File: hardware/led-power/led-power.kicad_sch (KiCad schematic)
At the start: 86 parts, among them J1 String1, J10 Conn_01x05_Male, J11 Qwiic, J12 Qwiic, J16 I2C Header, J17 IRQ, J2 String2, J3 String3, J4 String4, J5 String5, J6 String6, J7 String7, J8 String8, J9 PowerInput, Q1 Q_NMOS_GDS, Q2 Q_NMOS_GDS, Q3 Q_NMOS_GDS, Q4 Q_NMOS_GDS, Q5 Q_NMOS_GDS, Q6 Q_NMOS_GDS, Q7 Q_NMOS_GDS, Q8 Q_NMOS_GDS, U1 MCP6V51, U10 L78L05ACZ-AP, U11 MCP1501, U12 LM317_TO-220, U2 MCP6V51, U3 MCP6V51, U4 MCP6V51, U5 MCP6V51, U6 MCP6V51, U7 MCP6V51, U8 MCP6V51, U9 STM32G030Fx

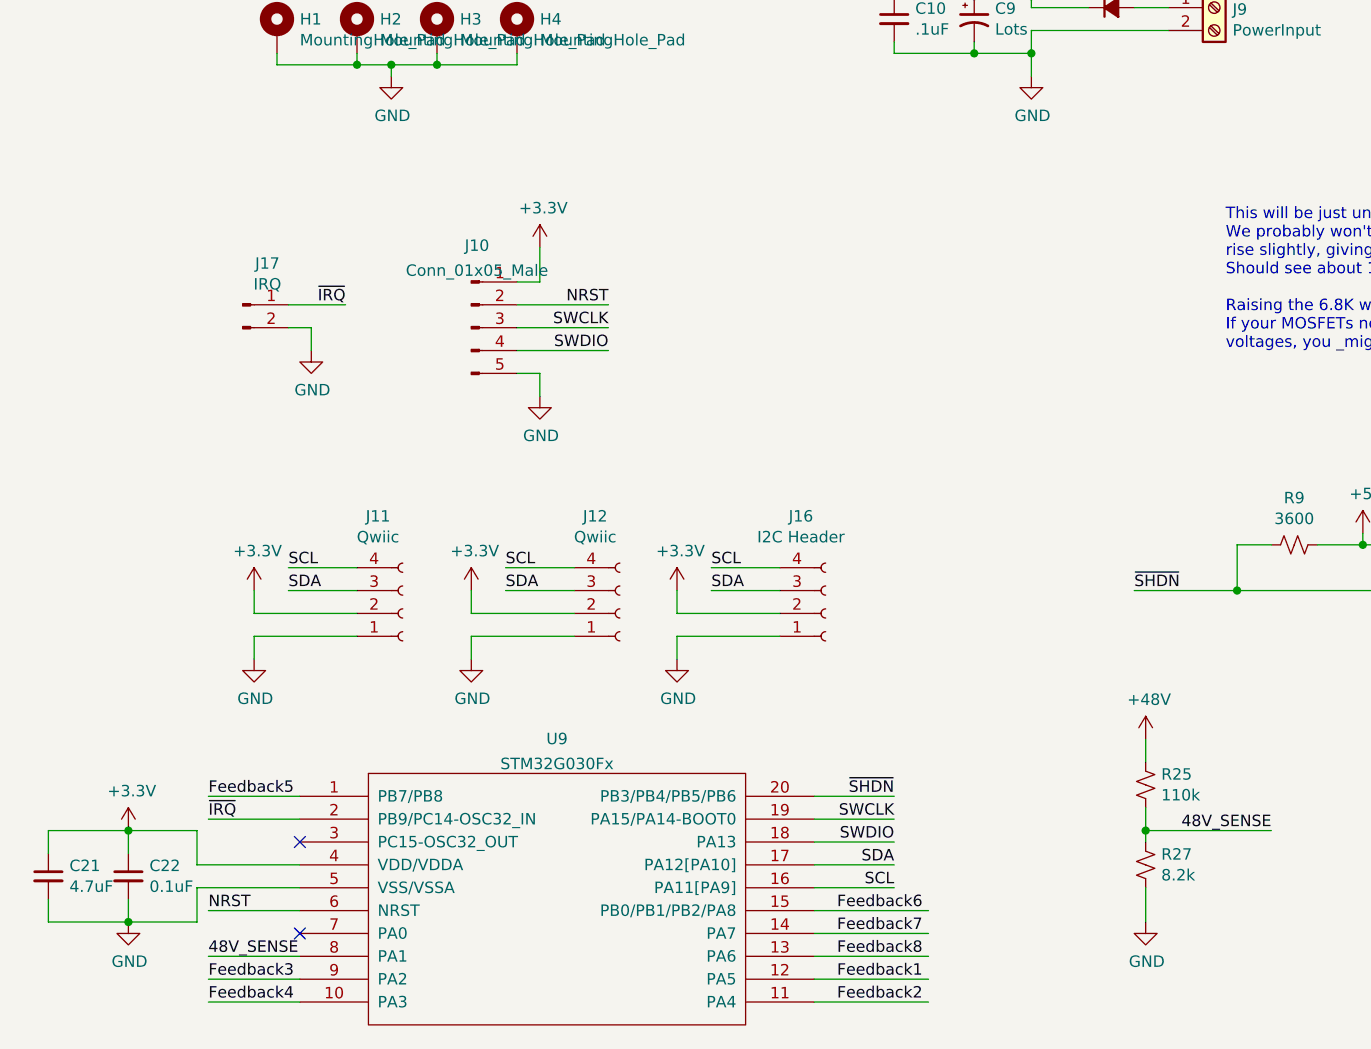
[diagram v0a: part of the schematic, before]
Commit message: Use a BJT to pull down the /IRQ line.
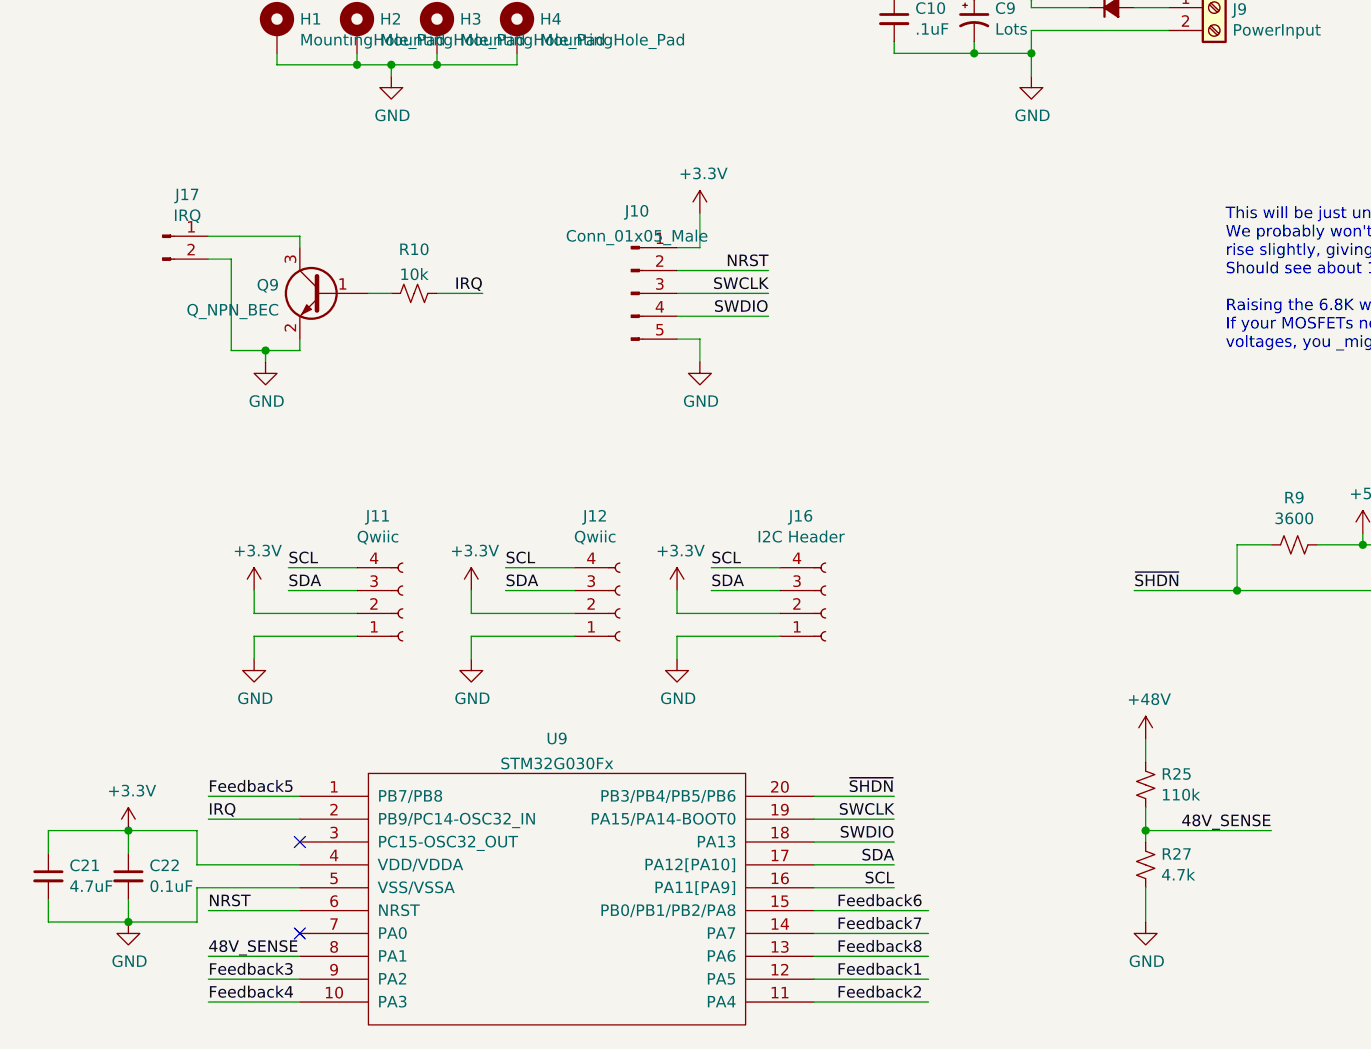
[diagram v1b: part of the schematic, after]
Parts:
- added Q9: Q_NPN_BEC, Package_TO_SOT_SMD:SOT-23, symbol Device:Q_NPN_BEC
- added R10: 10k, Resistor_SMD:R_0805_2012Metric_Pad1.20x1.40mm_HandSolder, symbol Device:R_Small_US
- R27: value 8.2k -> 4.7k
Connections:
- net GND: now also Q9.2 (E)
- net ~{IRQ}: no longer names the net of J17.1 (Pin_1)
- net ~{IRQ}: now also Q9.3 (C); no longer U9.2 (PB9/PC14-OSC32_IN)
- new net: Q9.1 (B), R10.1
- new net IRQ: R10.2, U9.2 (PB9/PC14-OSC32_IN)
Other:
- moved on the sheet: J10, J17

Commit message: Convert all other mounting holes to non-pad variety.
Reroute a few traces to be shorter.
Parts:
- H1, H2, H3, H4: footprint Mounting_Holes:MountingHole_3.2mm_M3_Pad_Via -> MountingHole:MountingHole_3.2mm_M3; symbol Mechanical:MountingHole_Pad -> Mechanical:MountingHole
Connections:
- net GND: no longer H1.1, H2.1, H3.1, H4.1
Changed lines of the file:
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@@
   (junction (at 382.27 50.8) (diameter 0) (color 0 0 0 0)
   )
-  (junction (at 205.74 38.1) (diameter 0) (color 0 0 0 0)
-  )
   (junction (at 370.84 60.96) (diameter 0) (color 0 0 0 0)
   )
@@
   (junction (at 107.95 30.48) (diameter 0) (color 0 0 0 0)
   )
-  (junction (at 196.85 38.1) (diameter 0) (color 0 0 0 0)
-  )
   (junction (at 129.54 45.72) (diameter 0) (color 0 0 0 0)
   )
@@
   (junction (at 107.95 162.56) (diameter 0) (color 0 0 0 0)
   )
-  (junction (at 200.66 38.1) (diameter 0) (color 0 0 0 0)
-  )
   (junction (at 36.83 53.34) (diameter 0) (color 0 0 0 0)
   )
@@
     (stroke (width 0) (type default) (color 0 0 0 0))
   )
-  (wire (pts (xy 196.85 38.1) (xy 187.96 38.1))
-    (stroke (width 0) (type default) (color 0 0 0 0))
-  )
   (wire (pts (xy 363.22 104.14) (xy 363.22 107.95))
     (stroke (width 0) (type default) (color 0 0 0 0))
@@
     (stroke (width 0) (type default) (color 0 0 0 0))
   )
-  (wire (pts (xy 205.74 38.1) (xy 200.66 38.1))
-    (stroke (width 0) (type default) (color 0 0 0 0))
-  )
   (wire (pts (xy 129.54 153.67) (xy 129.54 154.94))
     (stroke (width 0) (type default) (color 0 0 0 0))
@@
     (stroke (width 0) (type default) (color 0 0 0 0))
   )
-  (wire (pts (xy 200.66 38.1) (xy 196.85 38.1))
-    (stroke (width 0) (type default) (color 0 0 0 0))
-  )
-  (wire (pts (xy 214.63 36.83) (xy 214.63 38.1))
-    (stroke (width 0) (type default) (color 0 0 0 0))
-  )
   (wire (pts (xy 190.5 121.92) (xy 180.34 121.92))
     (stroke (width 0) (type default) (color 0 0 0 0))
@@
     (stroke (width 0) (type default) (color 0 0 0 0))
   )
-  (wire (pts (xy 187.96 38.1) (xy 187.96 36.83))
-    (stroke (width 0) (type default) (color 0 0 0 0))
-  )
   (wire (pts (xy 101.6 92.71) (xy 120.65 92.71))
     (stroke (width 0) (type default) (color 0 0 0 0))
@@
     (stroke (width 0) (type default) (color 0 0 0 0))
   )
-  (wire (pts (xy 205.74 36.83) (xy 205.74 38.1))
-    (stroke (width 0) (type default) (color 0 0 0 0))
-  )
   (wire (pts (xy 58.42 118.11) (xy 54.61 118.11))
     (stroke (width 0) (type default) (color 0 0 0 0))
@@
     (stroke (width 0) (type default) (color 0 0 0 0))
   )
-  (wire (pts (xy 196.85 36.83) (xy 196.85 38.1))
-    (stroke (width 0) (type default) (color 0 0 0 0))
-  )
   (wire (pts (xy 101.6 41.91) (xy 102.87 41.91))
     (stroke (width 0) (type default) (color 0 0 0 0))
@@
     (stroke (width 0) (type default) (color 0 0 0 0))
   )
-  (wire (pts (xy 200.66 38.1) (xy 200.66 39.37))
-    (stroke (width 0) (type default) (color 0 0 0 0))
-  )
   (wire (pts (xy 120.65 138.43) (xy 120.65 134.62))
     (stroke (width 0) (type default) (color 0 0 0 0))
@@
     (stroke (width 0) (type default) (color 0 0 0 0))
   )
-  (wire (pts (xy 214.63 38.1) (xy 205.74 38.1))
-    (stroke (width 0) (type default) (color 0 0 0 0))
-  )
   (wire (pts (xy 90.17 53.34) (xy 107.95 53.34))
     (stroke (width 0) (type default) (color 0 0 0 0))
@@
     (pin "2")
   )
-  (symbol (lib_id "Mechanical:MountingHole_Pad") (at 187.96 34.29 0) (unit 1)
+  (symbol (lib_id "Mechanical:MountingHole") (at 187.96 34.29 0) (unit 1)
     (in_bom yes) (on_board yes)
     (property "Reference" "H1" (id 0) (at 190.5 33.0454 0)
@@
       (effects (font (size 1.27 1.27)) (justify left))
     )
-    (property "Footprint" "Mounting_Holes:MountingHole_3.2mm_M3_Pad_Via" (id 2) (at 187.96 34.29 0)
+    (property "Footprint" "MountingHole:MountingHole_3.2mm_M3" (id 2) (at 187.96 34.29 0)
       (effects (font (size 1.27 1.27)) hide)
     )
@@
       (effects (font (size 1.27 1.27)) hide)
     )
-    (pin "1")
   )
-  (symbol (lib_id "Mechanical:MountingHole_Pad") (at 196.85 34.29 0) (unit 1)
+  (symbol (lib_id "Mechanical:MountingHole") (at 196.85 34.29 0) (unit 1)
     (in_bom yes) (on_board yes)
     (property "Reference" "H2" (id 0) (at 199.39 33.0454 0)
@@
       (effects (font (size 1.27 1.27)) (justify left))
     )
-    (property "Footprint" "Mounting_Holes:MountingHole_3.2mm_M3_Pad_Via" (id 2) (at 196.85 34.29 0)
+    (property "Footprint" "MountingHole:MountingHole_3.2mm_M3" (id 2) (at 196.85 34.29 0)
       (effects (font (size 1.27 1.27)) hide)
     )
@@
       (effects (font (size 1.27 1.27)) hide)
     )
-    (pin "1")
   )
-  (symbol (lib_id "Mechanical:MountingHole_Pad") (at 205.74 34.29 0) (unit 1)
+  (symbol (lib_id "Mechanical:MountingHole") (at 205.74 34.29 0) (unit 1)
     (in_bom yes) (on_board yes)
     (property "Reference" "H3" (id 0) (at 208.28 33.0454 0)
@@
       (effects (font (size 1.27 1.27)) (justify left))
     )
-    (property "Footprint" "Mounting_Holes:MountingHole_3.2mm_M3_Pad_Via" (id 2) (at 205.74 34.29 0)
+    (property "Footprint" "MountingHole:MountingHole_3.2mm_M3" (id 2) (at 205.74 34.29 0)
       (effects (font (size 1.27 1.27)) hide)
     )
@@
       (effects (font (size 1.27 1.27)) hide)
     )
-    (pin "1")
   )
-  (symbol (lib_id "Mechanical:MountingHole_Pad") (at 214.63 34.29 0) (unit 1)
+  (symbol (lib_id "Mechanical:MountingHole") (at 214.63 34.29 0) (unit 1)
     (in_bom yes) (on_board yes)
     (property "Reference" "H4" (id 0) (at 217.17 33.0454 0)
@@
       (effects (font (size 1.27 1.27)) (justify left))
     )
-    (property "Footprint" "Mounting_Holes:MountingHole_3.2mm_M3_Pad_Via" (id 2) (at 214.63 34.29 0)
+    (property "Footprint" "MountingHole:MountingHole_3.2mm_M3" (id 2) (at 214.63 34.29 0)
       (effects (font (size 1.27 1.27)) hide)
     )
@@
       (effects (font (size 1.27 1.27)) hide)
     )
-    (pin "1")
   )
   (symbol (lib_id "Connector:Conn_01x02_Male") (at 120.65 29.21 0) (unit 1)
@@
     (pin "2")
   )
-  (symbol (lib_id "power:GND") (at 200.66 39.37 0) (unit 1)
-    (in_bom yes) (on_board yes)
-    (property "Reference" "#PWR0133" (id 0) (at 200.66 45.72 0)
-      (effects (font (size 1.27 1.27)) hide)
-    )
-    (property "Value" "GND" (id 1) (at 200.787 43.7642 0))
-    (property "Footprint" "" (id 2) (at 200.66 39.37 0)
-      (effects (font (size 1.27 1.27)) hide)
-    )
-    (property "Datasheet" "" (id 3) (at 200.66 39.37 0)
-      (effects (font (size 1.27 1.27)) hide)
-    )
-    (pin "1")
-  )
   (symbol (lib_id "Device:LED_Small") (at 58.42 25.4 90) (unit 1)
     (in_bom yes) (on_board yes)
@@
       (reference "#PWR0132") (unit 1) (value "+12V") (footprint "")
     )
-    (path "/00000000-0000-0000-0000-00005fb57a4f"
-      (reference "#PWR0133") (unit 1) (value "GND") (footprint "")
-    )
     (path "/44e731ea-b714-4f81-b99c-baf50fcf6a6a"
       (reference "#PWR0134") (unit 1) (value "GND") (footprint "")
@@
     )
     (path "/00000000-0000-0000-0000-00005fb16605"
-      (reference "H1") (unit 1) (value "MountingHole_Pad") (footprint "Mounting_Holes:MountingHole_3.2mm_M3_Pad_Via")
+      (reference "H1") (unit 1) (value "MountingHole_Pad") (footprint "MountingHole:MountingHole_3.2mm_M3")
     )
     (path "/00000000-0000-0000-0000-00005fb1786c"
-      (reference "H2") (unit 1) (value "MountingHole_Pad") (footprint "Mounting_Holes:MountingHole_3.2mm_M3_Pad_Via")
+      (reference "H2") (unit 1) (value "MountingHole_Pad") (footprint "MountingHole:MountingHole_3.2mm_M3")
     )
     (path "/00000000-0000-0000-0000-00005fb17f4f"
-      (reference "H3") (unit 1) (value "MountingHole_Pad") (footprint "Mounting_Holes:MountingHole_3.2mm_M3_Pad_Via")
+      (reference "H3") (unit 1) (value "MountingHole_Pad") (footprint "MountingHole:MountingHole_3.2mm_M3")
     )
     (path "/00000000-0000-0000-0000-00005fb18585"
-      (reference "H4") (unit 1) (value "MountingHole_Pad") (footprint "Mounting_Holes:MountingHole_3.2mm_M3_Pad_Via")
+      (reference "H4") (unit 1) (value "MountingHole_Pad") (footprint "MountingHole:MountingHole_3.2mm_M3")
     )
     (path "/00000000-0000-0000-0000-00005fab9bdd"
